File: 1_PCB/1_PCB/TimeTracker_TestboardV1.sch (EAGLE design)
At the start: 18 parts, among them IC1 7805DT, IC2 7805DT, J1 2908-05WB-MG, U1 WS2812B, U2 WS2812B, U3 WS2812B, U4 WS2812B

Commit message: fucvk u raj
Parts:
- added JP5: (no value), jumper:JP1Q
- added LED_12V1: (no value), led:LEDSML0805
- added R3: 560, rcl:R-EU_R0805
- added RESET1: (no value), switch-omron:10-XX
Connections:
- new net GND1: RESET1.S, RESET1.S1, U$1.RST
- new net N$12: JP5.2, U$1.VIN
- new net N$35: LED_12V1.A, R3.1
- net 5V: now also JP5.1
- net GND: now also LED_12V1.C, RESET1.P, RESET1.P1, U$1.GND, U$1.GND2
- net N$1: now also R3.2
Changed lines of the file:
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@@
 <part name="GND10" library="SparkFun" deviceset="GND" device=""/>
 <part name="JP4" library="pinhead" library_urn="urn:adsk.eagle:library:325" deviceset="PINHD-2X4" device="" package3d_urn="urn:adsk.eagle:package:22461/2"/>
+<part name="GND11" library="SparkFun" deviceset="GND" device=""/>
+<part name="GND12" library="SparkFun" deviceset="GND" device=""/>
+<part name="RESET1" library="switch-omron" library_urn="urn:adsk.eagle:library:377" deviceset="10-XX" device="" package3d_urn="urn:adsk.eagle:package:27496/1"/>
+<part name="R3" library="rcl" library_urn="urn:adsk.eagle:library:334" deviceset="R-EU_" device="R0805" package3d_urn="urn:adsk.eagle:package:23553/2" value="560"/>
+<part name="LED_12V1" library="led" library_urn="urn:adsk.eagle:library:259" deviceset="LED" device="SML0805" package3d_urn="urn:adsk.eagle:package:15830/1"/>
+<part name="GND36" library="supply1" library_urn="urn:adsk.eagle:library:371" deviceset="GND" device=""/>
+<part name="JP5" library="jumper" library_urn="urn:adsk.eagle:library:252" deviceset="JP1Q" device="" package3d_urn="urn:adsk.eagle:package:15455/1"/>
 </parts>
 <sheets>
@@
 <attribute name="VALUE" x="-214.63" y="66.04" size="1.778" layer="96"/>
 </instance>
+<instance part="GND11" gate="1" x="-20.32" y="15.24" smashed="yes">
+<attribute name="VALUE" x="-22.86" y="12.7" size="1.778" layer="96"/>
+</instance>
+<instance part="GND12" gate="1" x="48.26" y="12.7" smashed="yes">
+<attribute name="VALUE" x="45.72" y="10.16" size="1.778" layer="96"/>
+</instance>
+<instance part="RESET1" gate="1" x="-27.94" y="25.4" smashed="yes" rot="R270">
+<attribute name="NAME" x="-30.48" y="31.75" size="1.778" layer="95"/>
+<attribute name="VALUE" x="-24.765" y="29.21" size="1.778" layer="96"/>
+</instance>
+<instance part="R3" gate="G$1" x="-200.66" y="172.72" smashed="yes" rot="R90">
+<attribute name="NAME" x="-202.1586" y="168.91" size="1.778" layer="95" rot="R90"/>
+<attribute name="VALUE" x="-197.358" y="168.91" size="1.778" layer="96" rot="R90"/>
+</instance>
+<instance part="LED_12V1" gate="G$1" x="-200.66" y="157.48" smashed="yes">
+<attribute name="NAME" x="-197.104" y="152.908" size="1.778" layer="95" rot="R90"/>
+<attribute name="VALUE" x="-194.945" y="152.908" size="1.778" layer="96" rot="R90"/>
+</instance>
+<instance part="GND36" gate="1" x="-200.66" y="144.78" smashed="yes">
+<attribute name="VALUE" x="-203.2" y="142.24" size="1.778" layer="96"/>
+</instance>
+<instance part="JP5" gate="A" x="-10.16" y="7.62" smashed="yes">
+<attribute name="NAME" x="-12.7" y="2.54" size="1.778" layer="95" rot="R90"/>
+<attribute name="VALUE" x="-5.715" y="2.54" size="1.778" layer="96" rot="R90"/>
+</instance>
 </instances>
 <busses>
@@
 <wire x1="-83.82" y1="111.76" x2="-83.82" y2="109.22" width="0.1524" layer="91"/>
 <pinref part="U4" gate="G$1" pin="VSS"/>
+</segment>
+<segment>
+<pinref part="U$1" gate="G$1" pin="GND"/>
+<wire x1="-5.08" y1="20.32" x2="-20.32" y2="20.32" width="0.1524" layer="91"/>
+<pinref part="GND11" gate="1" pin="GND"/>
+<wire x1="-20.32" y1="20.32" x2="-20.32" y2="17.78" width="0.1524" layer="91"/>
+<wire x1="-33.02" y1="25.4" x2="-38.1" y2="25.4" width="0.1524" layer="91"/>
+<wire x1="-38.1" y1="25.4" x2="-38.1" y2="22.86" width="0.1524" layer="91"/>
+<wire x1="-38.1" y1="22.86" x2="-33.02" y2="22.86" width="0.1524" layer="91"/>
+<junction x="-38.1" y="22.86"/>
+<pinref part="RESET1" gate="1" pin="P"/>
+<pinref part="RESET1" gate="1" pin="P1"/>
+<wire x1="-43.18" y1="22.86" x2="-38.1" y2="22.86" width="0.1524" layer="91"/>
+<wire x1="-43.18" y1="22.86" x2="-43.18" y2="20.32" width="0.1524" layer="91"/>
+<wire x1="-43.18" y1="20.32" x2="-20.32" y2="20.32" width="0.1524" layer="91"/>
+<junction x="-20.32" y="20.32"/>
+</segment>
+<segment>
+<pinref part="U$1" gate="G$1" pin="GND2"/>
+<wire x1="27.94" y1="25.4" x2="48.26" y2="25.4" width="0.1524" layer="91"/>
+<pinref part="GND12" gate="1" pin="GND"/>
+<wire x1="48.26" y1="25.4" x2="48.26" y2="15.24" width="0.1524" layer="91"/>
+</segment>
+<segment>
+<pinref part="LED_12V1" gate="G$1" pin="C"/>
+<pinref part="GND36" gate="1" pin="GND"/>
+<wire x1="-200.66" y1="152.4" x2="-200.66" y2="147.32" width="0.1524" layer="91"/>
 </segment>
 </net>
@@
 <wire x1="-190.5" y1="187.96" x2="-195.58" y2="187.96" width="0.1524" layer="91"/>
 <junction x="-190.5" y="187.96"/>
-<wire x1="-195.58" y1="187.96" x2="-205.74" y2="187.96" width="0.1524" layer="91"/>
+<wire x1="-195.58" y1="187.96" x2="-200.66" y2="187.96" width="0.1524" layer="91"/>
+<wire x1="-200.66" y1="187.96" x2="-205.74" y2="187.96" width="0.1524" layer="91"/>
 <wire x1="-195.58" y1="160.02" x2="-195.58" y2="187.96" width="0.1524" layer="91"/>
 <junction x="-195.58" y="187.96"/>
+<pinref part="R3" gate="G$1" pin="2"/>
+<wire x1="-200.66" y1="177.8" x2="-200.66" y2="187.96" width="0.1524" layer="91"/>
+<junction x="-200.66" y="187.96"/>
 </segment>
 </net>
@@
 <junction x="-111.76" y="132.08"/>
 </segment>
+<segment>
+<pinref part="JP5" gate="A" pin="1"/>
+<wire x1="-10.16" y1="0" x2="-10.16" y2="-2.54" width="0.1524" layer="91"/>
+<label x="-10.16" y="-2.54" size="1.778" layer="95" rot="R180" xref="yes"/>
+</segment>
 </net>
 <net name="N$9" class="0">
@@
 </segment>
 </net>
+<net name="GND1" class="0">
+<segment>
+<wire x1="-17.78" y1="25.4" x2="-22.86" y2="25.4" width="0.1524" layer="91"/>
+<pinref part="RESET1" gate="1" pin="S"/>
+<pinref part="RESET1" gate="1" pin="S1"/>
+<pinref part="U$1" gate="G$1" pin="RST"/>
+<wire x1="-22.86" y1="22.86" x2="-17.78" y2="22.86" width="0.1524" layer="91"/>
+<wire x1="-17.78" y1="22.86" x2="-5.08" y2="22.86" width="0.1524" layer="91"/>
+<wire x1="-17.78" y1="25.4" x2="-17.78" y2="22.86" width="0.1524" layer="91"/>
+<junction x="-17.78" y="22.86"/>
+</segment>
+</net>
+<net name="N$35" class="0">
+<segment>
+<pinref part="R3" gate="G$1" pin="1"/>
+<pinref part="LED_12V1" gate="G$1" pin="A"/>
+<wire x1="-200.66" y1="167.64" x2="-200.66" y2="160.02" width="0.1524" layer="91"/>
+</segment>
+</net>
+<net name="N$12" class="0">
+<segment>
+<pinref part="JP5" gate="A" pin="2"/>
+<wire x1="-10.16" y1="15.24" x2="-10.16" y2="17.78" width="0.1524" layer="91"/>
+<pinref part="U$1" gate="G$1" pin="VIN"/>
+<wire x1="-10.16" y1="17.78" x2="-5.08" y2="17.78" width="0.1524" layer="91"/>
+</segment>
+</net>

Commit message: First Commit Mitun
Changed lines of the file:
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@@
 <?xml version="1.0" encoding="utf-8"?>
 <!DOCTYPE eagle SYSTEM "eagle.dtd">
-<eagle version="9.3.0">
+<eagle version="9.2.2">
 <drawing>
 <settings>
@@
 </instance>
 <instance part="GND1" gate="1" x="-172.72" y="167.64" smashed="yes">
-<attribute name="VALUE" x="-175.26" y="165.1" size="1.778" layer="96"/>
+<attribute name="VALUE" x="-170.18" y="167.64" size="1.778" layer="96"/>
 </instance>
 <instance part="GND3" gate="1" x="-205.74" y="175.26" smashed="yes">
@@
 </instance>
 <instance part="IC2" gate="A1" x="-170.18" y="160.02" smashed="yes">
-<attribute name="NAME" x="-177.8" y="165.735" size="1.778" layer="95"/>
+<attribute name="NAME" x="-167.64" y="163.195" size="1.778" layer="95"/>
 <attribute name="VALUE" x="-177.8" y="163.195" size="1.778" layer="96"/>
 </instance>

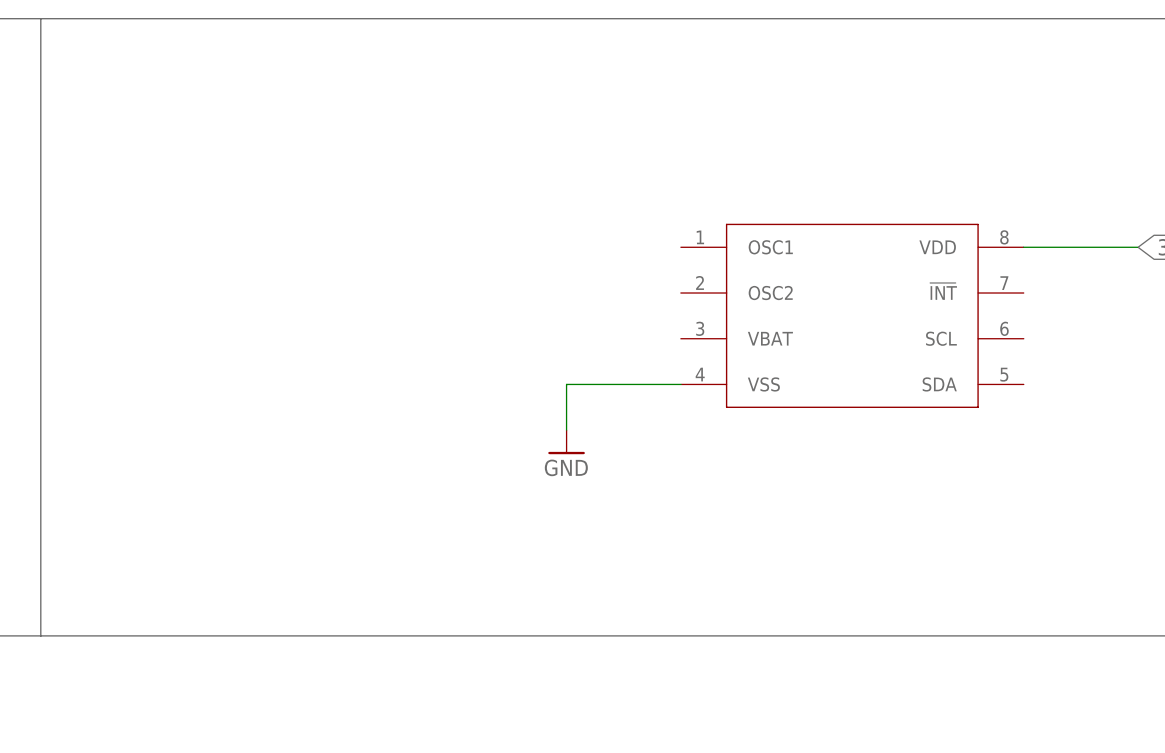
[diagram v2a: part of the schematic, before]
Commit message: Battery Holder and Oscillator Added to circtuit
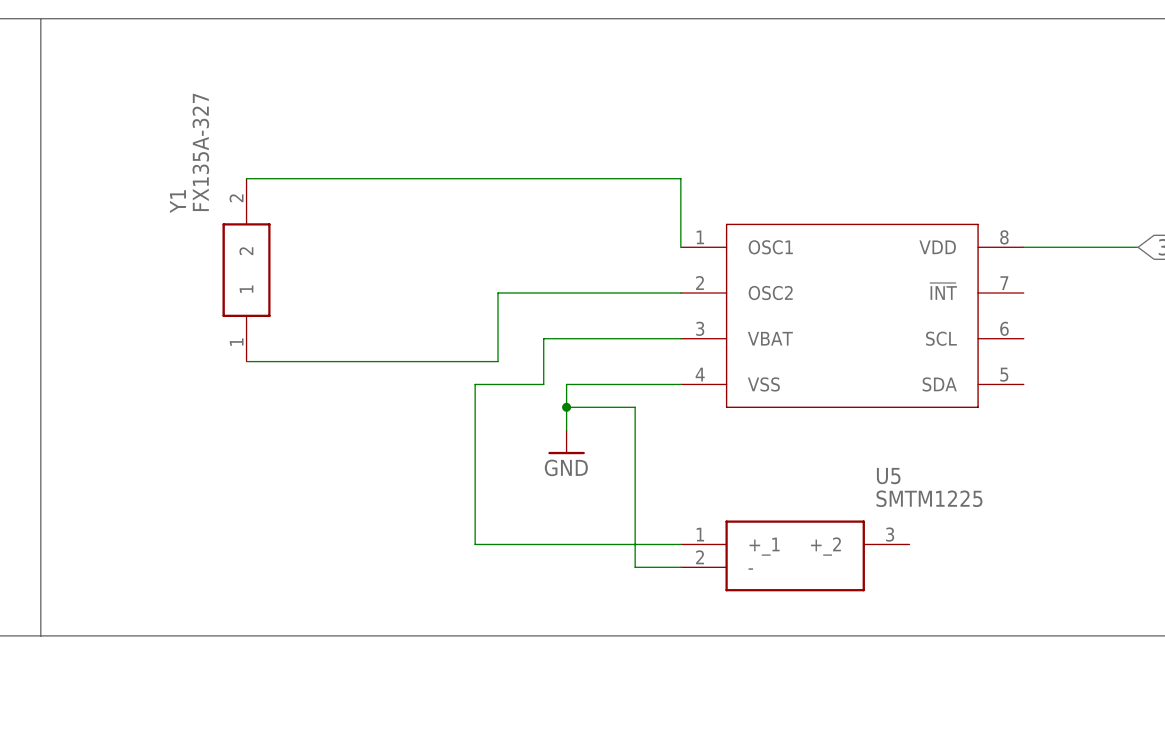
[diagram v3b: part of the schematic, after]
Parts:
- added U5: SMTM1225, SamacSys_Parts:SMTM1225
- added Y1: FX135A-327, SamacSys_Parts:FX135A-327
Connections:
- new net N$14: U$2.OSC1, Y1.2
- new net N$15: U$2.OSC2, Y1.1
- new net N$16: U$2.VBAT, U5.+_1
- net GND: now also U5.-
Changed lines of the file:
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@@
 <part name="GND36" library="supply1" library_urn="urn:adsk.eagle:library:371" deviceset="GND" device=""/>
 <part name="JP5" library="jumper" library_urn="urn:adsk.eagle:library:252" deviceset="JP1Q" device="" package3d_urn="urn:adsk.eagle:package:15455/1"/>
+<part name="Y1" library="SamacSys_Parts" deviceset="FX135A-327" device=""/>
+<part name="U5" library="SamacSys_Parts" deviceset="SMTM1225" device=""/>
 </parts>
 <sheets>
@@
 <attribute name="VALUE" x="-5.715" y="2.54" size="1.778" layer="96" rot="R90"/>
 </instance>
+<instance part="Y1" gate="G$1" x="17.78" y="167.64" smashed="yes" rot="R90">
+<attribute name="NAME" x="10.16" y="184.15" size="1.778" layer="95" rot="R90" align="center-left"/>
+<attribute name="VALUE" x="12.7" y="184.15" size="1.778" layer="96" rot="R90" align="center-left"/>
+</instance>
+<instance part="U5" gate="G$1" x="66.04" y="147.32" smashed="yes">
+<attribute name="NAME" x="87.63" y="154.94" size="1.778" layer="95" align="center-left"/>
+<attribute name="VALUE" x="87.63" y="152.4" size="1.778" layer="96" align="center-left"/>
+</instance>
 </instances>
 <busses>
@@
 <pinref part="U$2" gate="G$1" pin="VSS"/>
 <wire x1="66.04" y1="165.1" x2="53.34" y2="165.1" width="0.1524" layer="91"/>
-<wire x1="53.34" y1="165.1" x2="53.34" y2="160.02" width="0.1524" layer="91"/>
+<wire x1="53.34" y1="165.1" x2="53.34" y2="162.56" width="0.1524" layer="91"/>
 <pinref part="GND5" gate="1" pin="GND"/>
+<wire x1="53.34" y1="162.56" x2="53.34" y2="160.02" width="0.1524" layer="91"/>
+<wire x1="53.34" y1="162.56" x2="60.96" y2="162.56" width="0.1524" layer="91"/>
+<wire x1="60.96" y1="162.56" x2="60.96" y2="144.78" width="0.1524" layer="91"/>
+<junction x="53.34" y="162.56"/>
+<pinref part="U5" gate="G$1" pin="-"/>
+<wire x1="60.96" y1="144.78" x2="66.04" y2="144.78" width="0.1524" layer="91"/>
 </segment>
 <segment>
@@
 </segment>
 </net>
+<net name="N$14" class="0">
+<segment>
+<pinref part="Y1" gate="G$1" pin="2"/>
+<wire x1="17.78" y1="187.96" x2="66.04" y2="187.96" width="0.1524" layer="91"/>
+<pinref part="U$2" gate="G$1" pin="OSC1"/>
+<wire x1="66.04" y1="187.96" x2="66.04" y2="180.34" width="0.1524" layer="91"/>
+</segment>
+</net>
+<net name="N$15" class="0">
+<segment>
+<pinref part="Y1" gate="G$1" pin="1"/>
+<wire x1="17.78" y1="167.64" x2="45.72" y2="167.64" width="0.1524" layer="91"/>
+<wire x1="45.72" y1="167.64" x2="45.72" y2="175.26" width="0.1524" layer="91"/>
+<pinref part="U$2" gate="G$1" pin="OSC2"/>
+<wire x1="45.72" y1="175.26" x2="66.04" y2="175.26" width="0.1524" layer="91"/>
+</segment>
+</net>
+<net name="N$16" class="0">
+<segment>
+<pinref part="U5" gate="G$1" pin="+_1"/>
+<wire x1="66.04" y1="147.32" x2="43.18" y2="147.32" width="0.1524" layer="91"/>
+<wire x1="43.18" y1="147.32" x2="43.18" y2="165.1" width="0.1524" layer="91"/>
+<wire x1="43.18" y1="165.1" x2="50.8" y2="165.1" width="0.1524" layer="91"/>
+<wire x1="50.8" y1="165.1" x2="50.8" y2="170.18" width="0.1524" layer="91"/>
+<pinref part="U$2" gate="G$1" pin="VBAT"/>
+<wire x1="50.8" y1="170.18" x2="66.04" y2="170.18" width="0.1524" layer="91"/>
+</segment>
+</net>

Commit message: Humidity and Temp Sensor
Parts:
- added C5: (no value), rcl:C-EUC0805
- added HM1: SI7021-A20, SamacSys_Parts:SI7021-A20
- added R1, R2: 10k, rcl:R-EU_R0805
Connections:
- new net N$18: HM1.SCL, R2.1
- new net SDA: HM1.SDA, R1.1
- net 3V3: now also C5.1, HM1.VDD, R1.2, R2.2
- net GND: now also C5.2, HM1.GND
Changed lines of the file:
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@@
 <part name="Y1" library="SamacSys_Parts" deviceset="FX135A-327" device=""/>
 <part name="U5" library="SamacSys_Parts" deviceset="SMTM1225" device=""/>
+<part name="HM1" library="SamacSys_Parts" deviceset="SI7021-A20" device=""/>
+<part name="C5" library="rcl" library_urn="urn:adsk.eagle:library:334" deviceset="C-EU" device="C0805" package3d_urn="urn:adsk.eagle:package:23617/2"/>
+<part name="GND13" library="supply1" library_urn="urn:adsk.eagle:library:371" deviceset="GND" device=""/>
+<part name="GND14" library="supply1" library_urn="urn:adsk.eagle:library:371" deviceset="GND" device=""/>
+<part name="R1" library="rcl" library_urn="urn:adsk.eagle:library:334" deviceset="R-EU_" device="R0805" package3d_urn="urn:adsk.eagle:package:23553/2" value="10k"/>
+<part name="R2" library="rcl" library_urn="urn:adsk.eagle:library:334" deviceset="R-EU_" device="R0805" package3d_urn="urn:adsk.eagle:package:23553/2" value="10k"/>
 </parts>
 <sheets>
@@
 <wire x1="167.64" y1="99.06" x2="167.64" y2="137.16" width="0.1524" layer="95"/>
 <wire x1="167.64" y1="137.16" x2="167.64" y2="205.74" width="0.1524" layer="95"/>
-<wire x1="167.64" y1="137.16" x2="-5.08" y2="137.16" width="0.1524" layer="95"/>
+<wire x1="167.64" y1="137.16" x2="58.42" y2="137.16" width="0.1524" layer="95"/>
+<wire x1="58.42" y1="137.16" x2="-5.08" y2="137.16" width="0.1524" layer="95"/>
 <wire x1="-236.22" y1="93.98" x2="-236.22" y2="137.16" width="0.1524" layer="95"/>
 <wire x1="-76.2" y1="93.98" x2="-236.22" y2="93.98" width="0.1524" layer="95"/>
 <wire x1="-76.2" y1="137.16" x2="-76.2" y2="93.98" width="0.1524" layer="95"/>
+<wire x1="58.42" y1="93.98" x2="-76.2" y2="93.98" width="0.1524" layer="95"/>
+<wire x1="58.42" y1="137.16" x2="58.42" y2="93.98" width="0.1524" layer="95"/>
 </plain>
 <instances>
@@
 <attribute name="NAME" x="87.63" y="154.94" size="1.778" layer="95" align="center-left"/>
 <attribute name="VALUE" x="87.63" y="152.4" size="1.778" layer="96" align="center-left"/>
+</instance>
+<instance part="HM1" gate="G$1" x="-20.32" y="116.84" smashed="yes">
+<attribute name="NAME" x="6.35" y="124.46" size="1.778" layer="95" align="center-left"/>
+<attribute name="VALUE" x="6.35" y="121.92" size="1.778" layer="96" align="center-left"/>
+</instance>
+<instance part="C5" gate="G$1" x="22.86" y="109.22" smashed="yes">
+<attribute name="NAME" x="24.384" y="109.601" size="1.778" layer="95"/>
+<attribute name="VALUE" x="24.384" y="104.521" size="1.778" layer="96"/>
+</instance>
+<instance part="GND13" gate="1" x="-27.94" y="99.06" smashed="yes">
+<attribute name="VALUE" x="-30.48" y="96.52" size="1.778" layer="96"/>
+</instance>
+<instance part="GND14" gate="1" x="22.86" y="99.06" smashed="yes">
+<attribute name="VALUE" x="20.32" y="96.52" size="1.778" layer="96"/>
+</instance>
+<instance part="R1" gate="G$1" x="-24.13" y="122.428" smashed="yes" rot="R90">
+<attribute name="NAME" x="-25.6286" y="118.618" size="1.778" layer="95" rot="R90"/>
+<attribute name="VALUE" x="-20.828" y="118.618" size="1.778" layer="96" rot="R90"/>
+</instance>
+<instance part="R2" gate="G$1" x="14.224" y="122.682" smashed="yes" rot="R90">
+<attribute name="NAME" x="12.7254" y="118.872" size="1.778" layer="95" rot="R90"/>
+<attribute name="VALUE" x="17.526" y="118.872" size="1.778" layer="96" rot="R90"/>
 </instance>
 </instances>
@@
 <wire x1="104.14" y1="180.34" x2="116.84" y2="180.34" width="0.1524" layer="91"/>
 <label x="116.84" y="180.34" size="1.778" layer="95" xref="yes"/>
+</segment>
+<segment>
+<pinref part="HM1" gate="G$1" pin="VDD"/>
+<wire x1="10.16" y1="114.3" x2="22.86" y2="114.3" width="0.1524" layer="91"/>
+<label x="30.48" y="114.3" size="1.778" layer="95" xref="yes"/>
+<pinref part="C5" gate="G$1" pin="1"/>
+<wire x1="22.86" y1="114.3" x2="30.48" y2="114.3" width="0.1524" layer="91"/>
+<wire x1="22.86" y1="111.76" x2="22.86" y2="114.3" width="0.1524" layer="91"/>
+<junction x="22.86" y="114.3"/>
+</segment>
+<segment>
+<wire x1="-27.94" y1="129.54" x2="-24.13" y2="129.54" width="0.1524" layer="91"/>
+<pinref part="R1" gate="G$1" pin="2"/>
+<wire x1="-24.13" y1="129.54" x2="15.24" y2="129.54" width="0.1524" layer="91"/>
+<wire x1="-24.13" y1="127.508" x2="-24.13" y2="129.54" width="0.1524" layer="91"/>
+<pinref part="R2" gate="G$1" pin="2"/>
+<wire x1="14.224" y1="127.762" x2="15.24" y2="127.762" width="0.1524" layer="91"/>
+<wire x1="15.24" y1="127.762" x2="15.24" y2="129.54" width="0.1524" layer="91"/>
+<junction x="-24.13" y="129.54"/>
+<label x="-27.94" y="129.54" size="1.778" layer="95" rot="R180" xref="yes"/>
 </segment>
 </net>
@@
 <pinref part="GND36" gate="1" pin="GND"/>
 <wire x1="-200.66" y1="152.4" x2="-200.66" y2="147.32" width="0.1524" layer="91"/>
+</segment>
+<segment>
+<pinref part="HM1" gate="G$1" pin="GND"/>
+<wire x1="-20.32" y1="114.3" x2="-27.94" y2="114.3" width="0.1524" layer="91"/>
+<wire x1="-27.94" y1="114.3" x2="-27.94" y2="101.6" width="0.1524" layer="91"/>
+<pinref part="GND13" gate="1" pin="GND"/>
+</segment>
+<segment>
+<pinref part="C5" gate="G$1" pin="2"/>
+<pinref part="GND14" gate="1" pin="GND"/>
+<wire x1="22.86" y1="104.14" x2="22.86" y2="101.6" width="0.1524" layer="91"/>
 </segment>
 </net>
@@
 </segment>
 </net>
+<net name="SDA" class="0">
+<segment>
+<pinref part="HM1" gate="G$1" pin="SDA"/>
+<wire x1="-20.32" y1="116.84" x2="-24.13" y2="116.84" width="0.1524" layer="91"/>
+<label x="-30.48" y="116.84" size="1.778" layer="95" rot="R180" xref="yes"/>
+<pinref part="R1" gate="G$1" pin="1"/>
+<wire x1="-24.13" y1="116.84" x2="-30.48" y2="116.84" width="0.1524" layer="91"/>
+<wire x1="-24.13" y1="117.348" x2="-24.13" y2="116.84" width="0.1524" layer="91"/>
+<junction x="-24.13" y="116.84"/>
+<wire x1="-24.13" y1="116.84" x2="-24.13" y2="116.586" width="0.1524" layer="91"/>
+</segment>
+</net>
+<net name="N$18" class="0">
+<segment>
+<pinref part="HM1" gate="G$1" pin="SCL"/>
+<wire x1="10.16" y1="116.84" x2="15.24" y2="116.84" width="0.1524" layer="91"/>
+<label x="22.86" y="116.84" size="1.778" layer="95" xref="yes"/>
+<pinref part="R2" gate="G$1" pin="1"/>
+<wire x1="15.24" y1="116.84" x2="22.86" y2="116.84" width="0.1524" layer="91"/>
+<wire x1="14.224" y1="117.602" x2="15.24" y2="117.602" width="0.1524" layer="91"/>
+<wire x1="15.24" y1="117.602" x2="15.24" y2="116.84" width="0.1524" layer="91"/>
+<junction x="15.24" y="116.84"/>
+</segment>
+</net>

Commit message: Nico addition and modifications
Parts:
- removed J1: 2908-05WB-MG, 2908-05WB-MG:2908-05WB-MG
- added JP6: USD_CONNECTOR, SparkFun-Connectors:USD_CONNECTOR
- added R6, R7, R8, R9: 100k, rcl:R-EU_R0805
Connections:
- removed net N$4: J1.DAT1
- removed net N$6: J1.DAT2
- removed net N$7: J1.DAT3/CD
- removed net N$8: J1.CMD
- new net !CS_3V3: JP6.!CS, R9.1
- new net CD: JP6.CD2
- new net CDSDSD: JP6.CD1, R8.1
- new net RSV@1: JP6.RSV@1, R6.1
- new net RSV@2: JP6.RSV@2, R7.1
- net 3V3: now also JP6.VCC, R6.2, R7.2, R9.2; no longer J1.VDD
- net 5V: now also R8.2
- net GND: now also JP6.GND, JP6.SHIELD@1, JP6.SHIELD@3; no longer J1.VSS
- net N$16: now also U5.+_2
- net SPIMISO: now also JP6.DO
- net SPIMOSI: now also JP6.DI; no longer J1.DAT0
- net SPISCK: now also JP6.SCK; no longer J1.CLK
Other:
- note added: "100KΩ is the max Sandisk recommends"
- note added: "Remove shootthrough current on unused CMOS inputs"
